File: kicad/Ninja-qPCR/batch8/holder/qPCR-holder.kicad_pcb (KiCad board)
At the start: 2 copper layers, 94 x 58 mm, 0 parts

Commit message: order batch8
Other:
- board text added: "94x58mm"
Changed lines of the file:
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@@
   (general
     (thickness 1.6)
-    (drawings 219)
+    (drawings 220)
     (tracks 0)
     (zones 0)
@@
     (uvia_drill 0.1)
   )
+  (gr_text 94x58mm (at 122 69.02) (layer Dwgs.User)
+    (effects (font (size 1 1) (thickness 0.15)))
+  )
   (gr_text https://github.com/hisashin/Ninja-qPCR (at 165.650074 121.5) (layer F.SilkS)

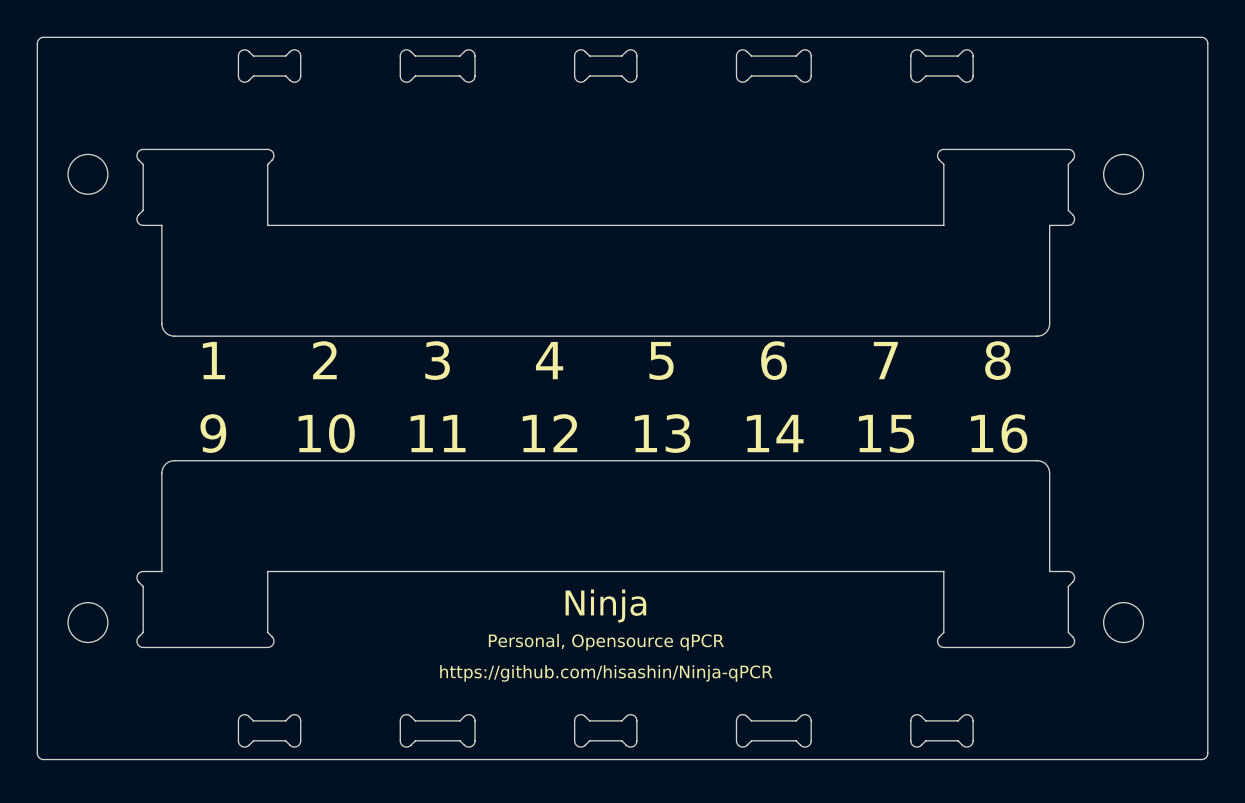
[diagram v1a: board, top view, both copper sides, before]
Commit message: ordered batch8 and got feedback
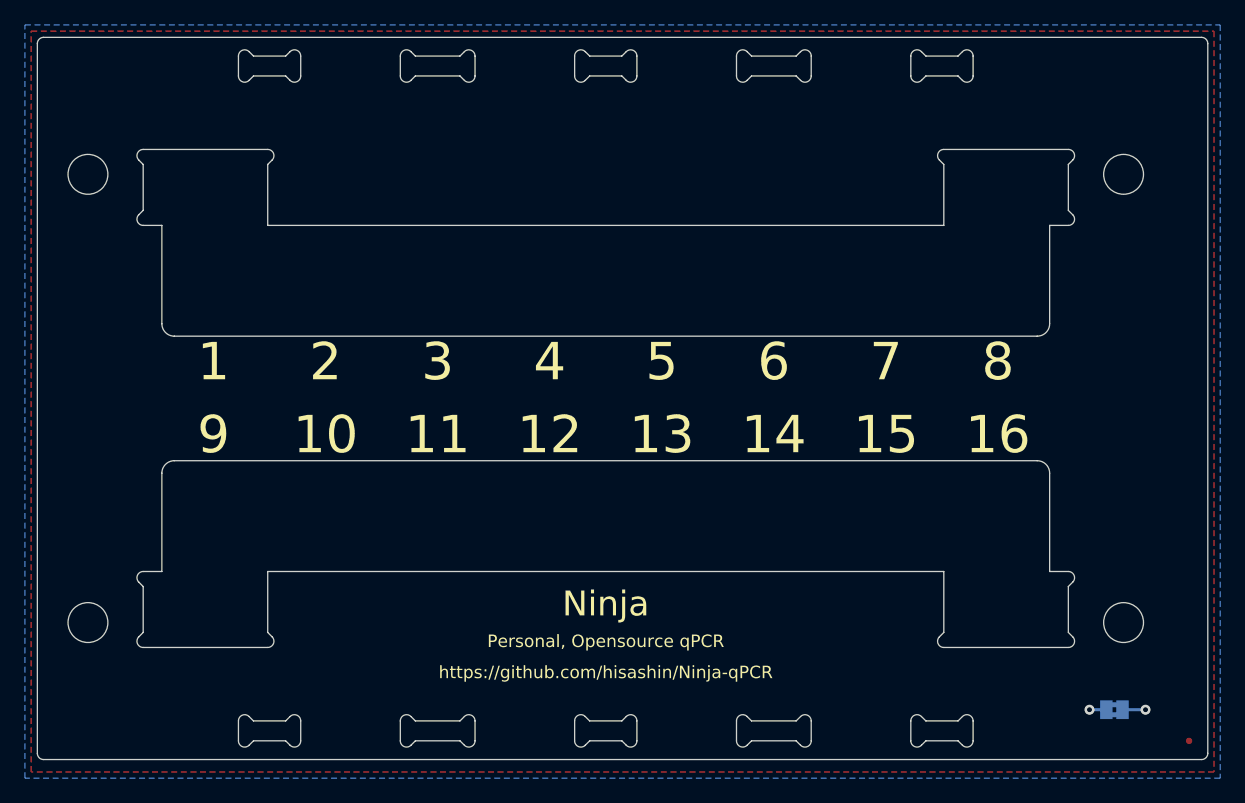
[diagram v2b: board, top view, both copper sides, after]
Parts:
- added FID1: Fiducial, Fiducials:Fiducial_0.5mm_Dia_1mm_Outer, F.Cu at (212.5, 127.0)
- added JP1: Jumper_2_Bridged, Jumper:SolderJumper-2_P1.3mm_Bridged2Bar_Pad1.0x1.5mm, B.Cu at (206.5, 124.5)
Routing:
- net GND: track 0.00 -> 3.20 mm, vias 0 -> 2
- added copper zone on B.Cu, net GND
- added copper zone on F.Cu, net GND
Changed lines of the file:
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@@
     (thickness 1.6)
     (drawings 220)
-    (tracks 0)
+    (tracks 4)
     (zones 0)
-    (modules 0)
-    (nets 1)
+    (modules 2)
+    (nets 2)
   )
   (page A4)
@@
       (usegerberattributes false)
       (usegerberadvancedattributes true)
-      (creategerberjobfile true)
+      (creategerberjobfile false)
       (excludeedgelayer true)
       (linewidth 0.100000)
@@
   )
   (net 0 "")
+  (net 1 GND)
   (net_class Default "This is the default net class."
     (clearance 0.2)
@@
     (uvia_dia 0.3)
     (uvia_drill 0.1)
-  )
-  (gr_text 94x58mm (at 122 69.02) (layer Dwgs.User)
+    (add_net GND)
+  )
+  (module Jumper:SolderJumper-2_P1.3mm_Bridged2Bar_Pad1.0x1.5mm (layer B.Cu)
+    (at 206.5 124.5)
+    (descr "SMD Solder Jumper, 1x1.5mm Pads, 0.3mm gap, bridged with 2 copper strips")
+    (tags "solder jumper open")
+    (attr virtual)
+    (fp_text reference JP1 (at 0 1.8) (layer B.SilkS) hide
+      (effects (font (size 1 1) (thickness 0.15)) (justify mirror))
+    )
+    (fp_text value Jumper_2_Bridged (at 0 -1.9) (layer B.Fab) hide
+      (effects (font (size 1 1) (thickness 0.15)) (justify mirror))
+    )
+    (fp_line (start -1.4 -1) (end -1.4 1) (layer B.SilkS) (width 0.12))
+    (fp_line (start 1.4 -1) (end -1.4 -1) (layer B.SilkS) (width 0.12))
+    (fp_line (start 1.4 1) (end 1.4 -1) (layer B.SilkS) (width 0.12))
+    (fp_line (start -1.4 1) (end 1.4 1) (layer B.SilkS) (width 0.12))
+    (fp_line (start -1.65 1.25) (end 1.65 1.25) (layer B.CrtYd) (width 0.05))
+    (fp_line (start -1.65 1.25) (end -1.65 -1.25) (layer B.CrtYd) (width 0.05))
+    (fp_line (start 1.65 -1.25) (end 1.65 1.25) (layer B.CrtYd) (width 0.05))
+    (fp_line (start 1.65 -1.25) (end -1.65 -1.25) (layer B.CrtYd) (width 0.05))
+    (fp_poly (pts (xy -0.25 -0.2) (xy 0.25 -0.2) (xy 0.25 -0.6) (xy -0.25 -0.6)) (layer B.Cu) (width 0))
+    (fp_poly (pts (xy -0.25 0.6) (xy 0.25 0.6) (xy 0.25 0.2) (xy -0.25 0.2)) (layer B.Cu) (width 0))
+    (pad 1 smd rect (at -0.65 0) (size 1 1.5) (layers B.Cu B.Mask)
+      (net 1 GND))
+    (pad 2 smd rect (at 0.65 0) (size 1 1.5) (layers B.Cu B.Mask)
+      (net 1 GND))
+  )
+  (module Fiducials:Fiducial_0.5mm_Dia_1mm_Outer (layer F.Cu)
+    (at 212.5 127)
+    (descr "Circular Fiducial, 0.5mm bare copper top; 1mm keepout (Level C)")
+    (tags marker)
+    (attr virtual)
+    (fp_text reference FID1 (at 0 -1.5) (layer F.SilkS) hide
+      (effects (font (size 1 1) (thickness 0.15)))
+    )
+    (fp_text value Fiducial (at 0 1.5) (layer F.Fab) hide
+      (effects (font (size 1 1) (thickness 0.15)))
+    )
+    (fp_text user %R (at 0 0) (layer F.Fab)
+      (effects (font (size 0.2 0.2) (thickness 0.04)))
+    )
+    (fp_circle (center 0 0) (end 0.5 0) (layer F.Fab) (width 0.1))
+    (fp_circle (center 0 0) (end 0.75 0) (layer F.CrtYd) (width 0.05))
+    (pad ~ smd circle (at 0 0) (size 0.5 0.5) (layers F.Cu F.Mask)
+      (solder_mask_margin 0.25) (clearance 0.25))
+  )
+  (gr_text 94x58mm (at 122 68.5) (layer Dwgs.User)
     (effects (font (size 1 1) (thickness 0.15)))
   )
@@
   (gr_line (start 201.3 85.601517) (end 202.8 85.601517) (layer Edge.Cuts) (width 0.1))
   (gr_line (start 201.3 93.498681) (end 201.3 85.601517) (layer Edge.Cuts) (width 0.1))
+  (via (at 209 124.5) (size 0.8) (drill 0.4) (layers F.Cu B.Cu) (net 1))
+  (via (at 204.5 124.5) (size 0.8) (drill 0.4) (layers F.Cu B.Cu) (net 1))
+  (segment (start 205.85 124.5) (end 204.5 124.5) (width 0.25) (layer B.Cu) (net 1) (status 10))
+  (segment (start 207.15 124.5) (end 209 124.5) (width 0.25) (layer B.Cu) (net 1) (status 10))
+  (zone (net 1) (net_name GND) (layer F.Cu) (hatch edge 0.508)
+    (connect_pads (clearance 0.508))
+    (min_thickness 0.254)
+    (fill yes (arc_segments 32) (thermal_gap 0.508) (thermal_bridge_width 0.508))
+    (polygon
+      (pts
+        (xy 214.5 129.5) (xy 119.5 129.5) (xy 119.5 70) (xy 214.5 70)
+      )
+    )
+  )
+  (zone (net 1) (net_name GND) (layer B.Cu) (hatch edge 0.508)
+    (connect_pads (clearance 0.508))
+    (min_thickness 0.254)
+    (fill yes (arc_segments 32) (thermal_gap 0.508) (thermal_bridge_width 0.508))
+    (polygon
+      (pts
+        (xy 215 130) (xy 119 130) (xy 119 69.5) (xy 215 69.5)
+      )
+    )
+  )
 )
